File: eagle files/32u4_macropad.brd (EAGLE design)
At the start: 77.2 x 102.2 mm, 91 parts, among them J1 TYPE-C-31-M-12, Q1 16MHz, SW2 SWITCH-SMD-EVP-BB2A9B00

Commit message: Fixed gnd plane not reaching underglow led #3, routing revision
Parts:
- moved C6 1.82 mm to (13.0, 95.7)
- moved R3 0.48 mm to (12.9, 102.0)
- moved C12 0.24 mm to (27.9, 108.0)
- moved C9 0.24 mm to (17.2, 105.8)
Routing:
- net UNDGLOW: track 82.0 -> 77.6 mm
- net R0SWTCH: track 74.6 -> 75.5 mm
- net N$17: vias 2 -> 0
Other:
- board text added: "Awareness16 rev 1"

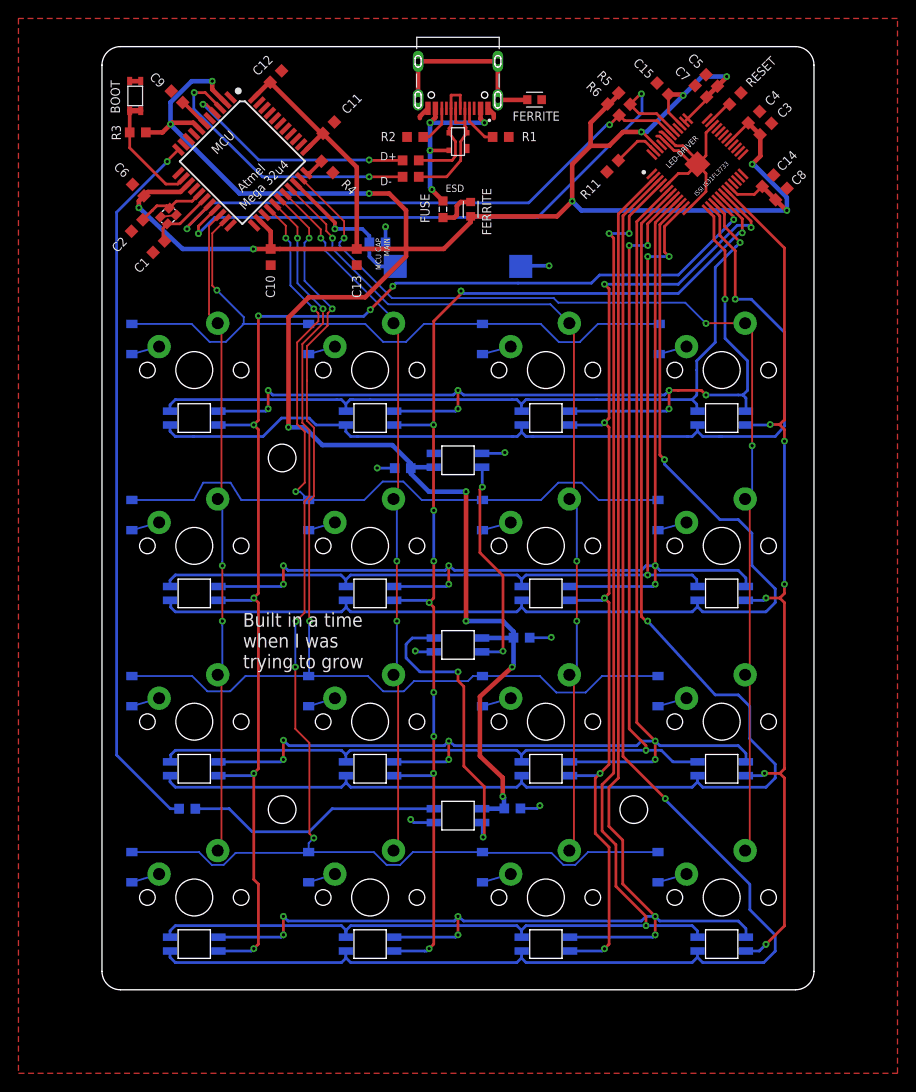
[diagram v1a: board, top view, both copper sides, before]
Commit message: Backlight led footprint fixed, started rerouting of those and other routing fixes
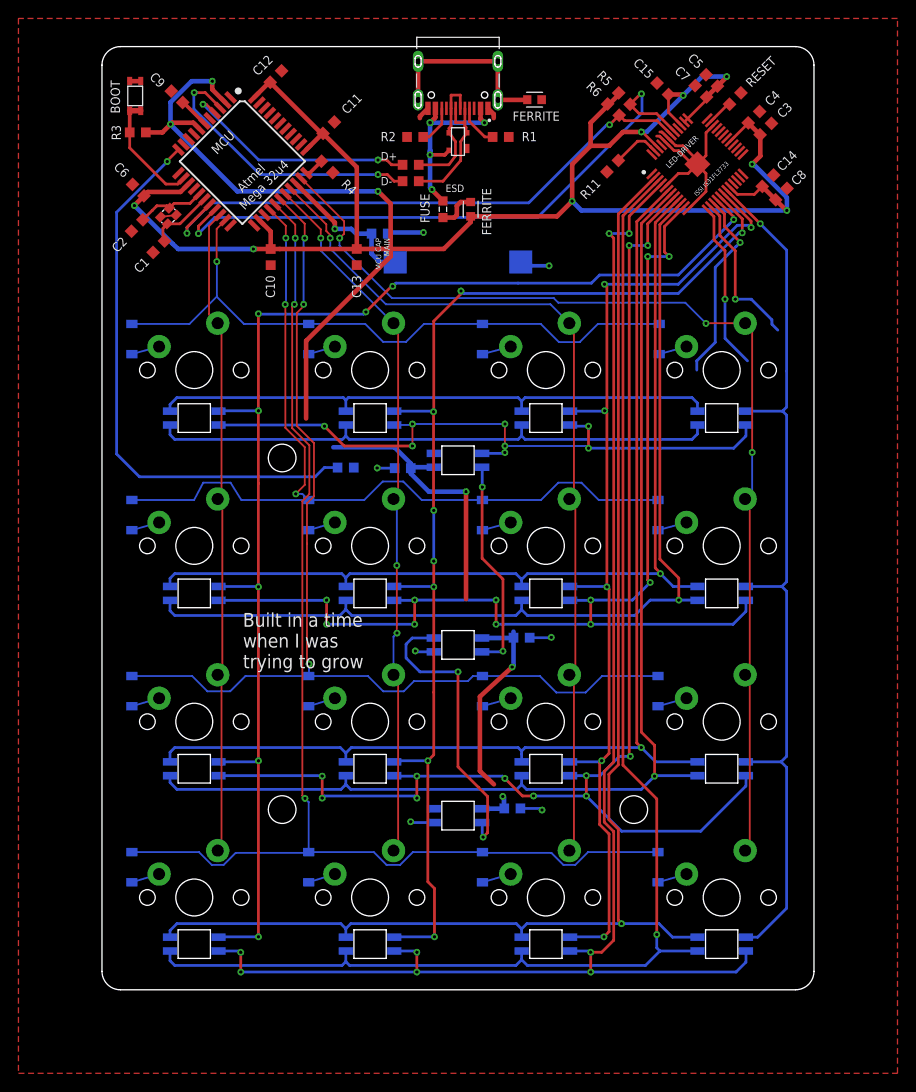
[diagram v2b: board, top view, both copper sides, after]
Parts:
- moved R12 40.8 mm to (35.5, 65.6)
- moved C16 0.98 mm to (39.1, 91.0)
- moved R7 0.48 mm to (42.5, 98.4)
- moved SP1 0.48 mm to (47.6, 87.9)
- moved R8 0.48 mm to (42.5, 96.7)
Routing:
- net N$7: track 27.9 -> 0.00 mm
- net R0GREEN: track 105.7 -> 80.3 mm, vias 8 -> 1
- net VCC: track 333.6 -> 311.4 mm, vias 16 -> 14
- net R3GREEN: track 166.1 -> 145.1 mm, vias 6 -> 1
- net R1BLUE: track 104.6 -> 125.4 mm, vias 3 -> 11
- net R0RED: track 100.6 -> 80.1 mm
- net R2GREEN: track 142.9 -> 124.0 mm, vias 6 -> 1
- net R2BLUE: track 124.9 -> 143.7 mm, vias 3 -> 11
- net R1GREEN: track 121.5 -> 103.1 mm, vias 6 -> 1
- net UNDGLOW: track 77.6 -> 61.1 mm
- net R2RED: track 142.5 -> 126.7 mm
- net R3RED: track 163.9 -> 148.8 mm
- net R1RED: track 121.0 -> 107.1 mm
- net R3BLUE: track 149.6 -> 159.9 mm, vias 3 -> 8
- net R0BLUE: track 85.9 -> 92.4 mm, vias 1 -> 8
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
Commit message: Rgb matrix leds routing done, underglow leds routing done
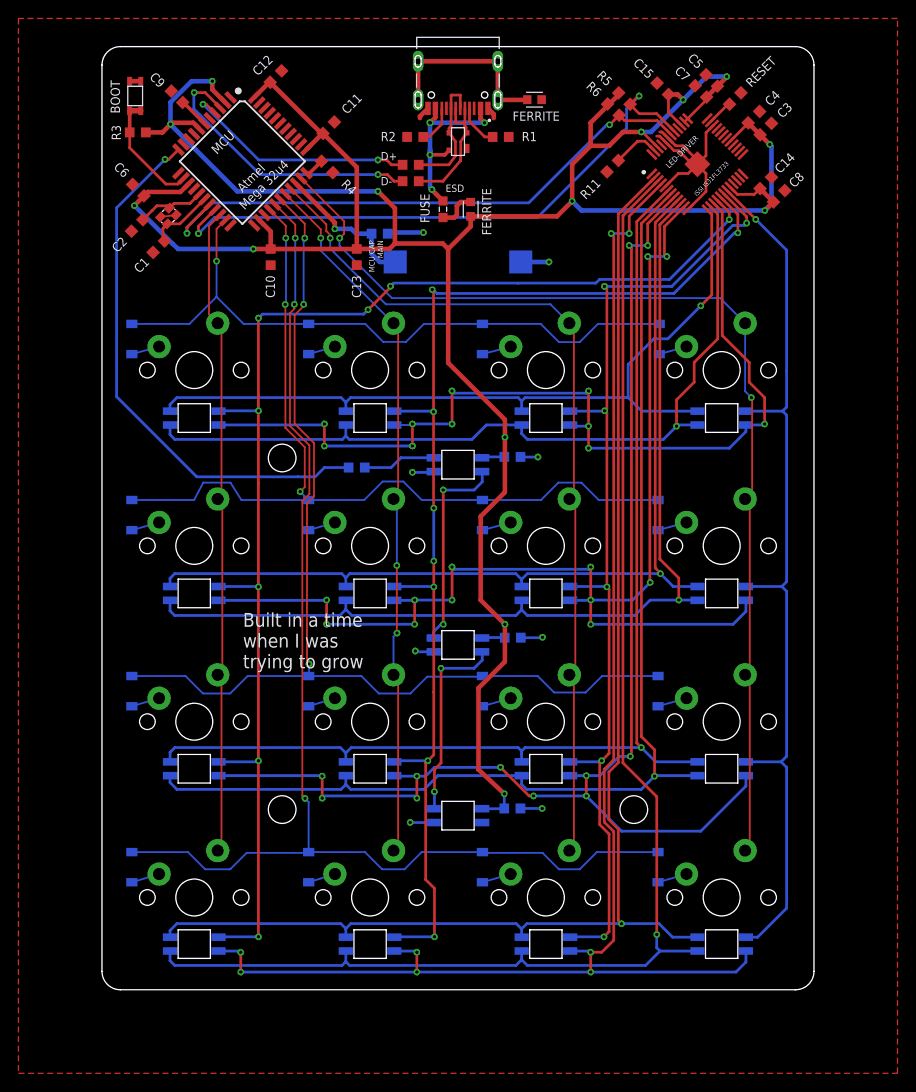
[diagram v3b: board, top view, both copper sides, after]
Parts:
- moved C19 11.9 mm to (53.5, 66.8), turned to 0 degrees
- moved R12 1.19 mm to (36.6, 65.6)
- moved C20 0.95 mm to (53.6, 47.2)
- moved UGLOW3 0.48 mm to (47.6, 65.9), turned to 0 degrees
- moved C14 0.34 mm to (81.0, 96.5)
- moved C8 0.34 mm to (82.4, 95.0)
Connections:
- net N$25: now also UGLOW1.P$4; no longer UGLOW3.P$4
- net N$39: now also UGLOW3.P$2; no longer UGLOW1.P$2
- net N$7: now also UGLOW3.P$4; no longer UGLOW1.P$4
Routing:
- net R0BLUE: track 92.4 -> 105.7 mm, vias 8 -> 10
- net N$39: track 32.1 -> 22.3 mm
- net R0RED: track 80.1 -> 88.4 mm
- net N$7: track 0.00 -> 7.91 mm
- net R0GREEN: track 80.3 -> 86.8 mm
- net R1BLUE: track 125.4 -> 129.8 mm, vias 11 -> 12
- net VCC: track 311.4 -> 307.2 mm
- net UNDGLOW: track 61.1 -> 58.9 mm
- net N$25: track 23.2 -> 21.3 mm
- net C1RGB: track 126.6 -> 128.3 mm
- net R3SWTCH: track 133.1 -> 134.4 mm
- net C2RGB: track 110.7 -> 109.4 mm
- net GND: track 54.3 -> 53.1 mm
- net C0RGB: track 143.5 -> 142.6 mm
- net R2BLUE: track 143.7 -> 144.6 mm
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
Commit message: REV 1 final commit
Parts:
- moved R1 0.72 mm to (53.0, 101.5)
- moved R7 0.53 mm to (42.3, 98.9)
- moved R8 0.53 mm to (42.3, 97.1)
- moved R2 0.48 mm to (42.5, 101.5)
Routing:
- net VCC: track 307.2 -> 294.1 mm, vias 14 -> 13
- net GND: track 53.1 -> 50.9 mm
- net UNDGLOW: track 58.9 -> 60.7 mm
- net N$24: track 29.4 -> 30.6 mm
- net R2BLUE: track 144.6 -> 145.7 mm
- net N$6: track 31.1 -> 30.1 mm
- net VBUS: track 21.7 -> 20.7 mm
- net R3BLUE: track 159.4 -> 160.2 mm
- net C3SWTCH: track 115.5 -> 114.9 mm
- net C1RGB: track 128.3 -> 128.2 mm, vias 8 -> 6
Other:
- board text added: "D+"
- board text added: "D-"
- board text removed: "D+ D-"
